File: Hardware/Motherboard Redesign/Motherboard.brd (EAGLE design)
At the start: 108 x 90.2 mm, 115 parts, among them J1 U.FL, J2 AVR_SPI_PRG_6PTH, U2 ATMEGA328P_PDIP, U3_MUX 74HC4052D,653, U4_MUX 74HC4052D,653, U5_MUX 74HC4052D,653, U6_MUX 74HC4052D,653, U7_MUX 74HC4052D,653, Y1 8MHz

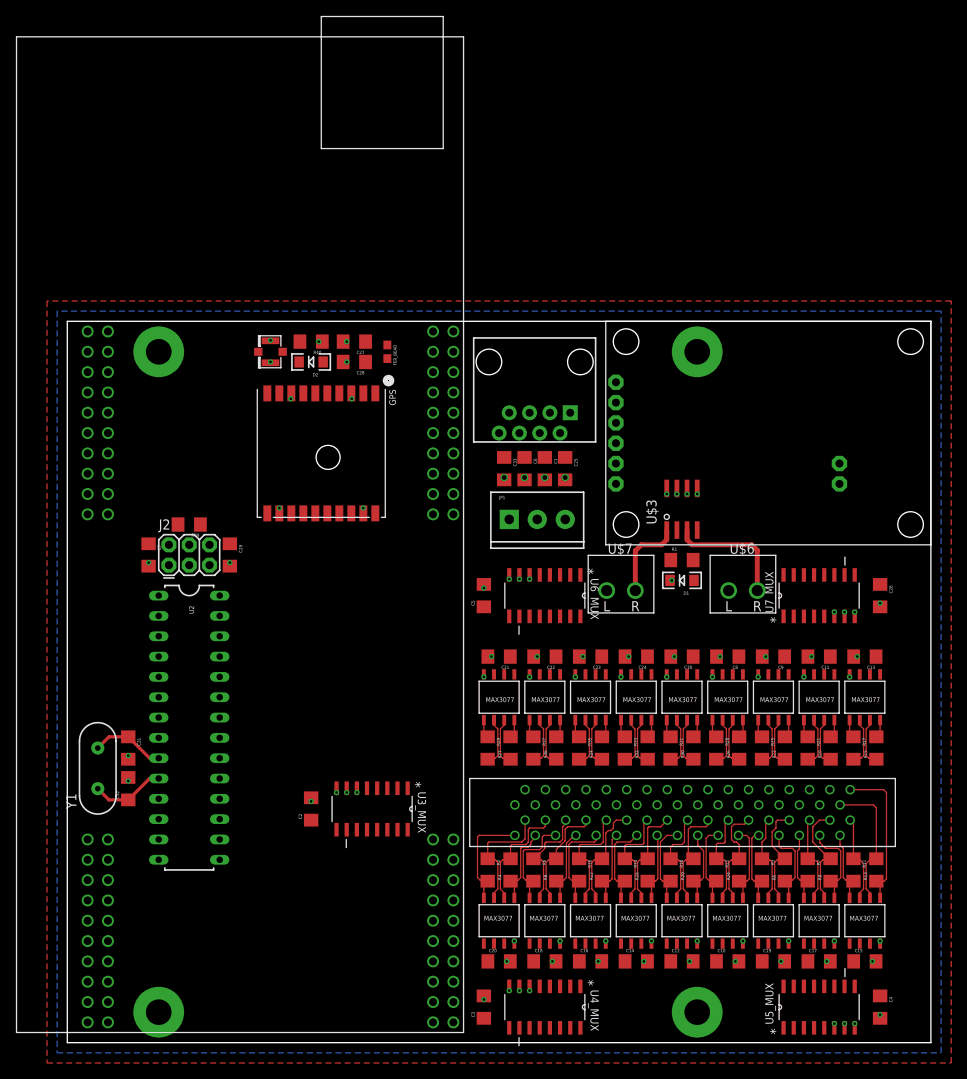
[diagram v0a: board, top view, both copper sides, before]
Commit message: connected wires
25% done
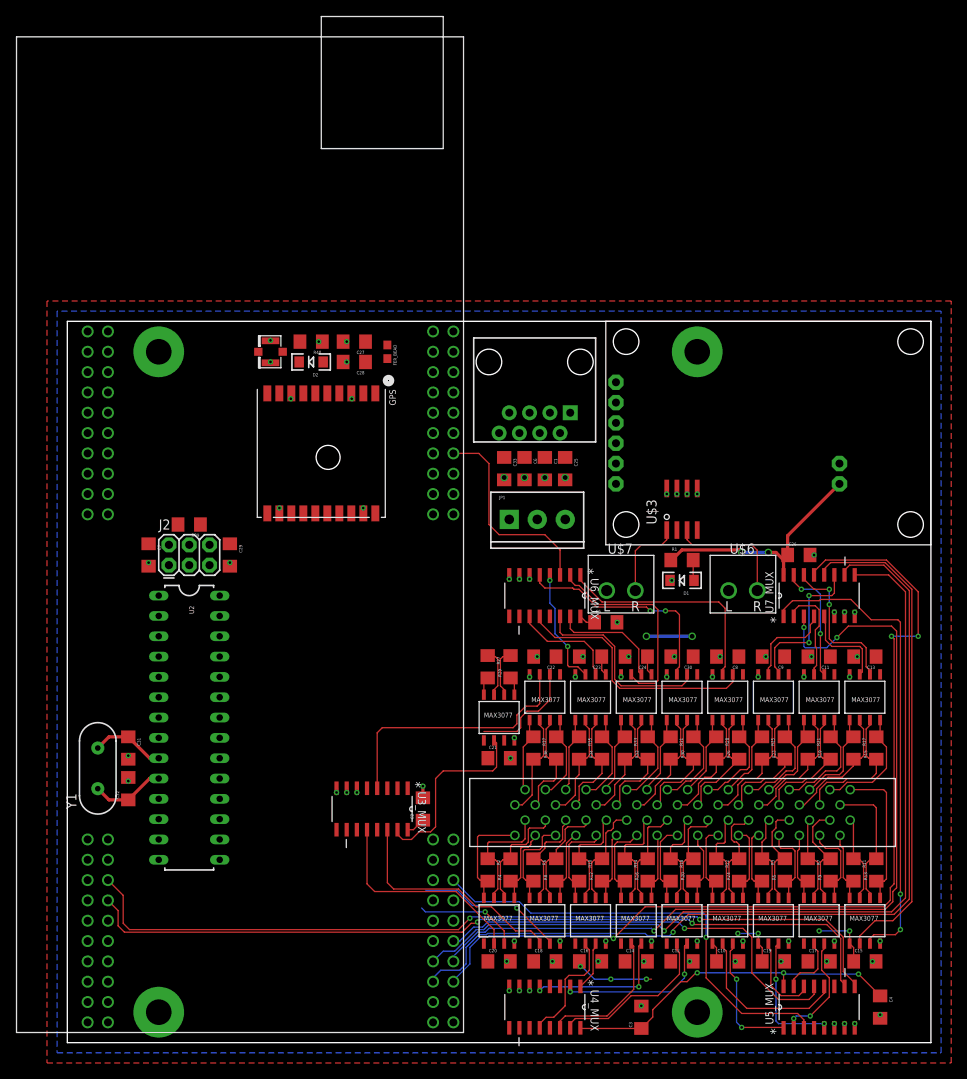
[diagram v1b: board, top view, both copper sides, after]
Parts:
- moved C3 19.7 mm to (71.8, 3.17)
- moved C5 15.6 mm to (67.3, 52.5), turned to 0 degrees
- moved C2 14.0 mm to (44.5, 29.2)
- moved C21 12.7 mm to (54.0, 35.6), turned to 0 degrees
- moved C26 11.4 mm to (91.4, 61.0), turned to 0 degrees
- moved R27 10.6 mm to (52.5, 47.0), turned to 270 degrees
- moved R29 10.6 mm to (55.4, 47.0), turned to 90 degrees
- moved RS-485-2 2.54 mm to (54.0, 40.6), turned to 0 degrees
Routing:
- net U7RX: track 0.00 -> 118.3 mm, vias 0 -> 3
- net U7_MUX_S0: track 0.00 -> 114.6 mm, vias 0 -> 1
- net U7TX: track 0.00 -> 109.5 mm, vias 0 -> 3
- net U7_MUX_S1: track 0.00 -> 108.5 mm, vias 0 -> 1
- net U5_MUX_S1: track 0.00 -> 105.2 mm, vias 0 -> 2
- net U5_MUX_S0: track 0.00 -> 102.2 mm, vias 0 -> 2
- net +5V: track 0.00 -> 78.4 mm, vias 0 -> 5
- net RS485_9_RX: track 0.00 -> 61.7 mm
- net RS485_9_TX: track 0.00 -> 60.5 mm, vias 0 -> 2
- net U5TX: track 0.00 -> 56.6 mm, vias 0 -> 1
- net U5RX: track 0.00 -> 54.0 mm, vias 0 -> 1
- net +3V3: track 0.00 -> 37.3 mm, vias 0 -> 9
- net RS485_17_TX: track 0.00 -> 33.1 mm
- net RS485_13_RX: track 0.00 -> 32.0 mm
- net RS485_2_RX: track 0.00 -> 29.1 mm
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
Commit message: wired everything
All wires done have some questions on some warnings and locations of
capaciters.
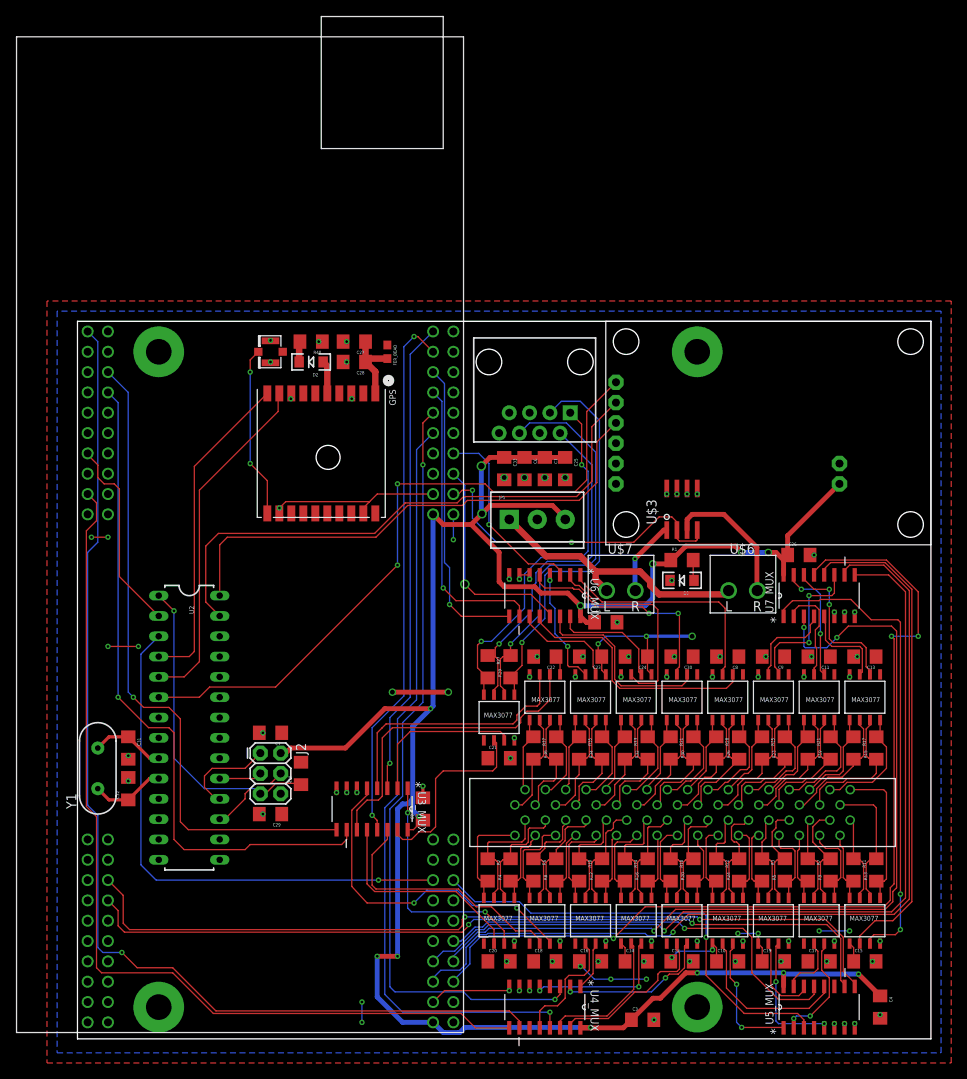
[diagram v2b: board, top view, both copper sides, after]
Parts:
- moved R39 34.1 mm to (29.2, 33.7), turned to 90 degrees
- moved C29 32.8 mm to (25.4, 28.6), turned to 180 degrees
- moved C7 26.9 mm to (25.4, 38.7), turned to 180 degrees
- moved J2 26.1 mm to (24.1, 36.2), turned to 270 degrees
- moved S2 0.64 mm to (11.4, 4.45)
- moved S4 0.64 mm to (78.7, 4.45)
- moved C3 0.35 mm to (71.9, 2.86), turned to 0 degrees
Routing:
- net +5V: track 78.4 -> 271.0 mm, vias 5 -> 14
- net U4_MUX_S0: track 0.00 -> 135.9 mm, vias 0 -> 1
- net U4_MUX_S1: track 0.00 -> 115.4 mm
- net U4TX: track 0.00 -> 97.2 mm, vias 0 -> 2
- net U4RX: track 0.00 -> 96.2 mm, vias 0 -> 1
- net DTR: track 0.00 -> 85.2 mm, vias 0 -> 2
- net U3_MUX_S0: track 0.00 -> 84.6 mm, vias 0 -> 1
- net U3_MUX_S1: track 0.00 -> 81.7 mm, vias 0 -> 1
- net IMU_TX: track 0.00 -> 72.2 mm
- net U3RX: track 0.00 -> 67.2 mm, vias 0 -> 2
- net U2RX: track 0.00 -> 66.8 mm, vias 0 -> 1
- net IMU_RX: track 0.00 -> 65.2 mm
- net U3TX: track 0.00 -> 59.5 mm, vias 0 -> 1
- net 18_TX+: track 2.29 -> 49.8 mm, vias 0 -> 1
- net GND: track 33.9 -> 79.2 mm, vias 78 -> 83
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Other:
- board size 108 x 90.2 mm -> 106.7 x 89.7 mm

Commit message: Enlarged power wires
Cleaned up wires as well
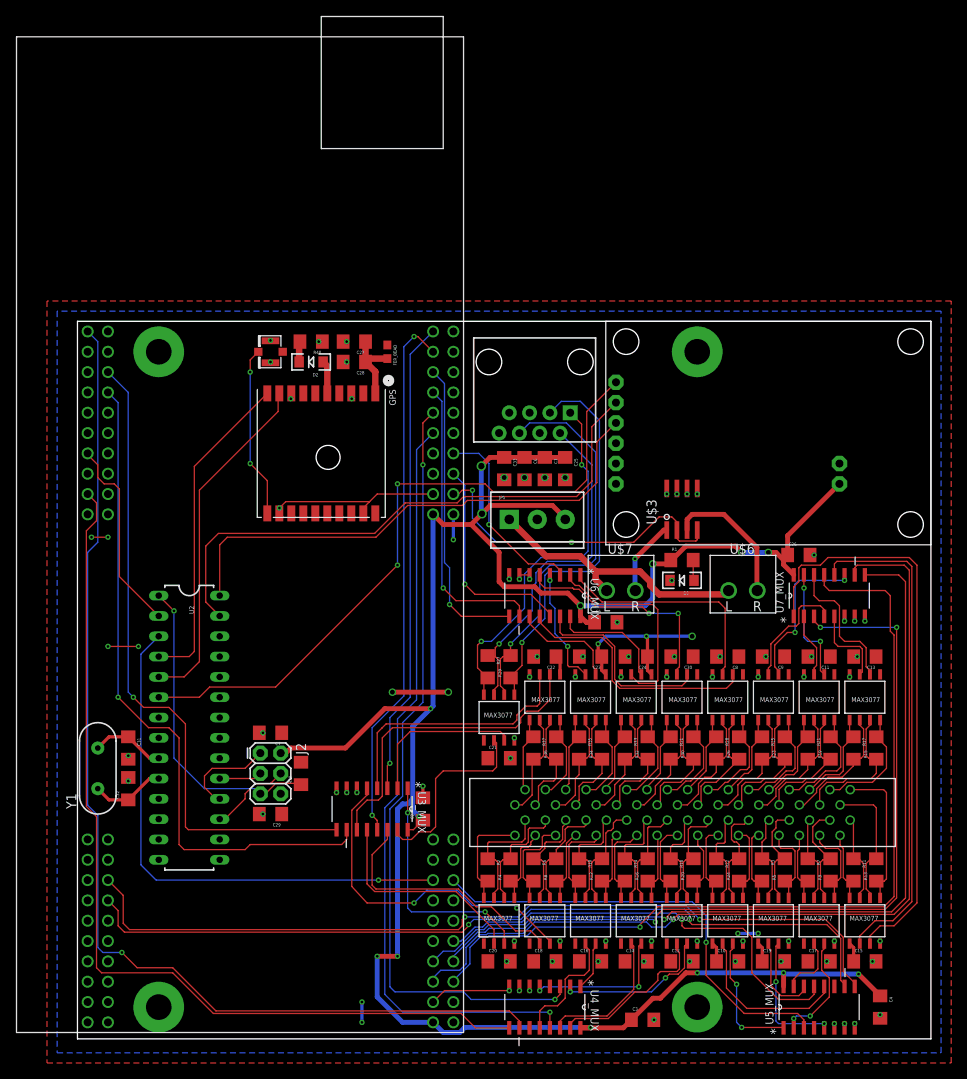
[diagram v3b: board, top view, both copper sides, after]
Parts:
- moved U7_MUX 1.27 mm to (95.2, 55.9)
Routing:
- net +3V3: track 63.3 -> 39.9 mm, vias 15 -> 8
- net RS485_9_TX: track 60.5 -> 72.8 mm, vias 2 -> 0
- net U7RX: track 118.3 -> 108.9 mm, vias 3 -> 1
- net RS485_11_TX: track 12.8 -> 8.04 mm
- net U7TX: track 109.5 -> 104.7 mm
- net RS485_12_TX: track 11.7 -> 14.7 mm
- net U5_MUX_S0: track 102.3 -> 103.9 mm
- net RS485_10_RX: track 19.0 -> 17.6 mm, vias 2 -> 0
- net U5RX: track 54.0 -> 55.3 mm
- net U5_MUX_S1: track 105.7 -> 106.8 mm
- net RS485_10_TX: track 11.4 -> 10.4 mm
- net U7_MUX_S1: track 108.5 -> 107.6 mm
- net RS485_9_RX: track 61.7 -> 62.6 mm
- net RS485_12_RX: track 19.5 -> 20.2 mm
- net RS485_11_RX: track 15.0 -> 14.4 mm

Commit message: wires changed
was bored
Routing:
- net GND: track 79.4 -> 72.4 mm, vias 83 -> 81
- net DTR: track 85.2 -> 86.0 mm
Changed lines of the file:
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@@
 <wire x1="47.14875" y1="6.50875" x2="55.245" y2="6.50875" width="0.1524" layer="1"/>
 <via x="5.08" y="49.53" extent="1-16" drill="0.3302" shape="square"/>
-<wire x1="5.08" y1="49.53" x2="8.89" y2="49.53" width="0.1524" layer="1"/>
+<wire x1="5.08" y1="49.53" x2="8.89" y2="49.53" width="0.4064" layer="1"/>
 <via x="8.89" y="49.53" extent="1-16" drill="0.3302" shape="square"/>
 <via x="3.01625" y="63.1825" extent="1-16" drill="0.3302" shape="square"/>
-<wire x1="3.01625" y1="63.1825" x2="5.08" y2="63.1825" width="0.1524" layer="1"/>
+<wire x1="3.01625" y1="63.1825" x2="5.08" y2="63.1825" width="0.4064" layer="1"/>
 <via x="5.08" y="63.1825" extent="1-16" drill="0.3302" shape="square"/>
-<wire x1="37.7825" y1="67.6275" x2="36.98875" y2="66.83375" width="0.1524" layer="1"/>
-<wire x1="45.72" y1="68.58" x2="38.735" y2="68.58" width="0.1524" layer="1"/>
-<wire x1="38.735" y1="68.58" x2="37.7825" y2="67.6275" width="0.1524" layer="1"/>
-<wire x1="37.7825" y1="67.6275" x2="27.305" y2="67.6275" width="0.1524" layer="1"/>
-<wire x1="27.305" y1="67.6275" x2="26.51125" y2="66.83375" width="0.1524" layer="1"/>
+<wire x1="37.7825" y1="67.6275" x2="36.98875" y2="66.83375" width="0.4064" layer="1"/>
+<wire x1="45.72" y1="68.58" x2="38.735" y2="68.58" width="0.4064" layer="1"/>
+<wire x1="38.735" y1="68.58" x2="37.7825" y2="67.6275" width="0.4064" layer="1"/>
+<wire x1="37.7825" y1="67.6275" x2="27.305" y2="67.6275" width="0.4064" layer="1"/>
+<wire x1="27.305" y1="67.6275" x2="26.51125" y2="66.83375" width="0.4064" layer="1"/>
 <wire x1="56.515" y1="58.4708" x2="57.785" y2="58.4708" width="0.1524" layer="1"/>
-<via x="47.625" y="43.815" extent="1-16" drill="0.6" shape="square"/>
-<wire x1="47.625" y1="43.815" x2="40.64" y2="43.815" width="0.6096" layer="1"/>
-<via x="40.64" y="43.815" extent="1-16" drill="0.6" shape="square"/>
 <wire x1="97.155" y1="53.2892" x2="97.155" y2="52.705" width="0.1524" layer="1"/>
 <via x="97.155" y="52.705" extent="1-16" drill="0.3302" shape="square"/>
@@
 <wire x1="39.6875" y1="41.75125" x2="45.4025" y2="41.75125" width="0.6096" layer="1"/>
 <via x="45.4025" y="41.75125" extent="1-16" drill="0.3302" shape="square"/>
-<wire x1="45.4025" y1="41.75125" x2="43.18" y2="39.52875" width="0.6096" layer="16"/>
-<wire x1="43.18" y1="39.52875" x2="43.18" y2="30.48" width="0.6096" layer="16"/>
 <wire x1="43.18" y1="30.48" x2="43.18" y2="29.05125" width="0.6096" layer="16"/>
 <wire x1="43.18" y1="29.05125" x2="43.97375" y2="28.2575" width="0.6096" layer="16"/>
@@
 <wire x1="89.535" y1="60.325" x2="89.535" y2="59.7408" width="0.6096" layer="1"/>
 <wire x1="89.535" y1="59.7408" x2="90.805" y2="58.4708" width="0.6096" layer="1"/>
+<wire x1="45.4025" y1="41.75125" x2="45.4025" y2="35.2425" width="0.6096" layer="16"/>
+<wire x1="45.4025" y1="35.2425" x2="43.18" y2="33.02" width="0.6096" layer="16"/>
+<wire x1="43.18" y1="33.02" x2="43.18" y2="30.48" width="0.6096" layer="16"/>
 </signal>
 <signal name="+12V">
@@
 <wire x1="39.6875" y1="6.0325" x2="39.6875" y2="29.36875" width="0.1524" layer="16"/>
 <wire x1="39.6875" y1="29.36875" x2="41.275" y2="30.95625" width="0.1524" layer="16"/>
-<wire x1="41.275" y1="30.95625" x2="41.275" y2="40.48125" width="0.1524" layer="16"/>
-<wire x1="41.275" y1="40.48125" x2="43.65625" y2="42.8625" width="0.1524" layer="16"/>
-<wire x1="43.65625" y1="42.8625" x2="43.65625" y2="74.13625" width="0.1524" layer="16"/>
+<wire x1="43.65625" y1="35.40125" x2="43.65625" y2="74.13625" width="0.1524" layer="16"/>
 <wire x1="43.65625" y1="74.13625" x2="45.72" y2="76.2" width="0.1524" layer="16"/>
 <wire x1="60.325" y1="1.8542" x2="60.325" y2="3.81" width="0.1524" layer="1"/>
 <via x="60.325" y="3.81" extent="1-16" drill="0.3302" shape="square"/>
+<wire x1="43.65625" y1="35.40125" x2="41.275" y2="33.02" width="0.1524" layer="16"/>
+<wire x1="41.275" y1="33.02" x2="41.275" y2="30.95625" width="0.1524" layer="16"/>
 </signal>
 <signal name="U4TX">
@@
 <wire x1="40.9575" y1="6.35" x2="40.3225" y2="6.985" width="0.1524" layer="16"/>
 <wire x1="40.3225" y1="6.985" x2="40.3225" y2="29.21" width="0.1524" layer="16"/>
-<wire x1="40.3225" y1="29.21" x2="41.91" y2="30.7975" width="0.1524" layer="16"/>
-<wire x1="41.91" y1="30.7975" x2="41.91" y2="40.005" width="0.1524" layer="16"/>
-<wire x1="41.91" y1="40.005" x2="44.45" y2="42.545" width="0.1524" layer="16"/>
-<wire x1="44.45" y1="42.545" x2="44.45" y2="72.23125" width="0.1524" layer="16"/>
+<wire x1="40.3225" y1="29.21" x2="41.75125" y2="30.63875" width="0.1524" layer="16"/>
+<wire x1="44.45" y1="35.56" x2="44.45" y2="72.23125" width="0.1524" layer="16"/>
 <via x="44.45" y="72.23125" extent="1-16" drill="0.3302" shape="square"/>
 <wire x1="44.45" y1="72.23125" x2="44.45" y2="77.47" width="0.1524" layer="1"/>
 <wire x1="44.45" y1="77.47" x2="45.72" y2="78.74" width="0.1524" layer="1"/>
+<wire x1="44.45" y1="35.56" x2="41.91" y2="33.02" width="0.1524" layer="16"/>
+<wire x1="41.91" y1="33.02" x2="41.91" y2="30.7975" width="0.1524" layer="16"/>
+<wire x1="41.91" y1="30.7975" x2="41.75125" y2="30.63875" width="0.1524" layer="16"/>
 </signal>
 <signal name="U7RX">
@@
 <wire x1="38.735" y1="27.78125" x2="38.1" y2="28.41625" width="0.1524" layer="1"/>
 <via x="38.1" y="28.41625" extent="1-16" drill="0.3302" shape="square"/>
-<wire x1="38.1" y1="28.41625" x2="38.1" y2="39.37" width="0.1524" layer="16"/>
-<wire x1="38.1" y1="39.37" x2="42.06875" y2="43.33875" width="0.1524" layer="16"/>
-<wire x1="42.06875" y1="43.33875" x2="42.06875" y2="86.995" width="0.1524" layer="16"/>
-<wire x1="42.06875" y1="86.995" x2="43.33875" y2="88.265" width="0.1524" layer="16"/>
-<via x="43.33875" y="88.265" extent="1-16" drill="0.3302" shape="square"/>
-<wire x1="43.33875" y1="88.265" x2="43.815" y2="88.265" width="0.1524" layer="1"/>
+<wire x1="38.1" y1="28.41625" x2="38.1" y2="54.61" width="0.1524" layer="16"/>
+<wire x1="38.1" y1="54.61" x2="41.275" y2="57.785" width="0.1524" layer="16"/>
+<wire x1="41.275" y1="57.785" x2="41.275" y2="86.36" width="0.1524" layer="16"/>
+<wire x1="41.275" y1="86.36" x2="43.18" y2="88.265" width="0.1524" layer="16"/>
+<via x="43.18" y="88.265" extent="1-16" drill="0.3302" shape="square"/>
+<wire x1="43.18" y1="88.265" x2="43.815" y2="88.265" width="0.1524" layer="1"/>
 <wire x1="43.815" y1="88.265" x2="45.72" y2="86.36" width="0.1524" layer="1"/>
 </signal>
@@
 <contactref element="U$5" pad="P11"/>
 <contactref element="U3_MUX" pad="3"/>
-<wire x1="40.005" y1="31.8008" x2="40.005" y2="34.6075" width="0.1524" layer="1"/>
-<wire x1="40.005" y1="34.6075" x2="40.3225" y2="34.925" width="0.1524" layer="1"/>
-<via x="40.3225" y="34.925" extent="1-16" drill="0.3302" shape="square"/>
-<wire x1="40.3225" y1="34.925" x2="40.3225" y2="40.64" width="0.1524" layer="16"/>
-<wire x1="40.3225" y1="40.64" x2="42.8625" y2="43.18" width="0.1524" layer="16"/>
-<wire x1="42.8625" y1="43.18" x2="42.8625" y2="86.0425" width="0.1524" layer="16"/>
-<wire x1="42.8625" y1="86.0425" x2="45.72" y2="88.9" width="0.1524" layer="16"/>
+<wire x1="40.005" y1="31.8008" x2="40.005" y2="36.98875" width="0.1524" layer="1"/>
+<wire x1="40.005" y1="36.98875" x2="40.3225" y2="37.30625" width="0.1524" layer="1"/>
+<via x="40.3225" y="37.30625" extent="1-16" drill="0.3302" shape="square"/>
+<wire x1="40.3225" y1="37.30625" x2="40.3225" y2="55.88" width="0.1524" layer="16"/>
+<wire x1="40.3225" y1="55.88" x2="41.91" y2="57.4675" width="0.1524" layer="16"/>
+<wire x1="41.91" y1="57.4675" x2="41.91" y2="85.09" width="0.1524" layer="16"/>
+<wire x1="41.91" y1="85.09" x2="45.72" y2="88.9" width="0.1524" layer="16"/>
 </signal>
 <signal name="U6_MUX_S0">
@@
 <wire x1="16.51" y1="43.18" x2="17.78" y2="44.45" width="0.1524" layer="1"/>
 <wire x1="17.78" y1="44.45" x2="26.035" y2="44.45" width="0.1524" layer="1"/>
-<wire x1="26.035" y1="44.45" x2="41.275" y2="59.69" width="0.1524" layer="1"/>
-<via x="41.275" y="59.69" extent="1-16" drill="0.3302" shape="square"/>
-<wire x1="41.275" y1="59.69" x2="41.275" y2="69.85" width="0.1524" layer="16"/>
-<via x="41.275" y="69.85" extent="1-16" drill="0.3302" shape="square"/>
-<wire x1="41.275" y1="69.85" x2="52.22875" y2="69.85" width="0.1524" layer="1"/>
+<wire x1="40.005" y1="69.85" x2="52.22875" y2="69.85" width="0.1524" layer="1"/>
 <wire x1="52.22875" y1="69.85" x2="53.18125" y2="68.8975" width="0.1524" layer="1"/>
 <wire x1="53.18125" y1="68.8975" x2="63.5" y2="68.8975" width="0.1524" layer="1"/>
+<via x="40.005" y="69.85" extent="1-16" drill="0.3302" shape="square"/>
+<wire x1="40.005" y1="69.85" x2="40.005" y2="58.42" width="0.1524" layer="16"/>
+<via x="40.005" y="58.42" extent="1-16" drill="0.3302" shape="square"/>
+<wire x1="40.005" y1="58.42" x2="26.035" y2="44.45" width="0.1524" layer="1"/>
 </signal>
 <signal name="OUT_1">
